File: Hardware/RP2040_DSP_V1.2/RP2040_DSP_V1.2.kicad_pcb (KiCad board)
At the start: 2 copper layers, 168.7 x 136.6 mm, 104 parts, among them J1 DC, J10 MIDI OUT, J11 MIDI IN, J12 OUTPUT, J13 Main, J2 EXP1, J3 EXP_2, J4 Daughter, J5 SW1, J6 SW2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

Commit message: [3D] Models updated
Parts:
- U12: footprint RP2040_DSP_Project_Library:128x64OLED -> DMME_Library:128x64OLED
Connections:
- RV8 pad : GNDD -> (no net)

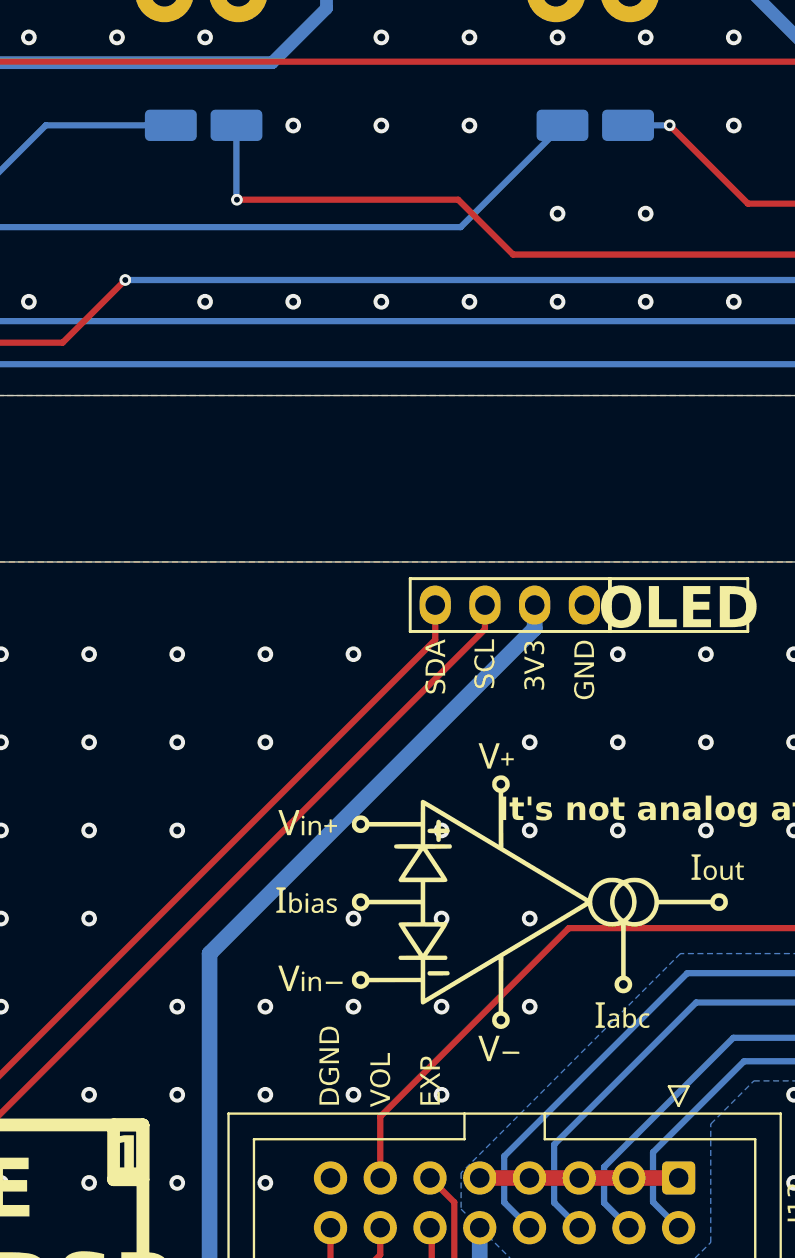
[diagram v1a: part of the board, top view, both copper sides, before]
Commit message: Added manufacturing files and BOM for V1.2
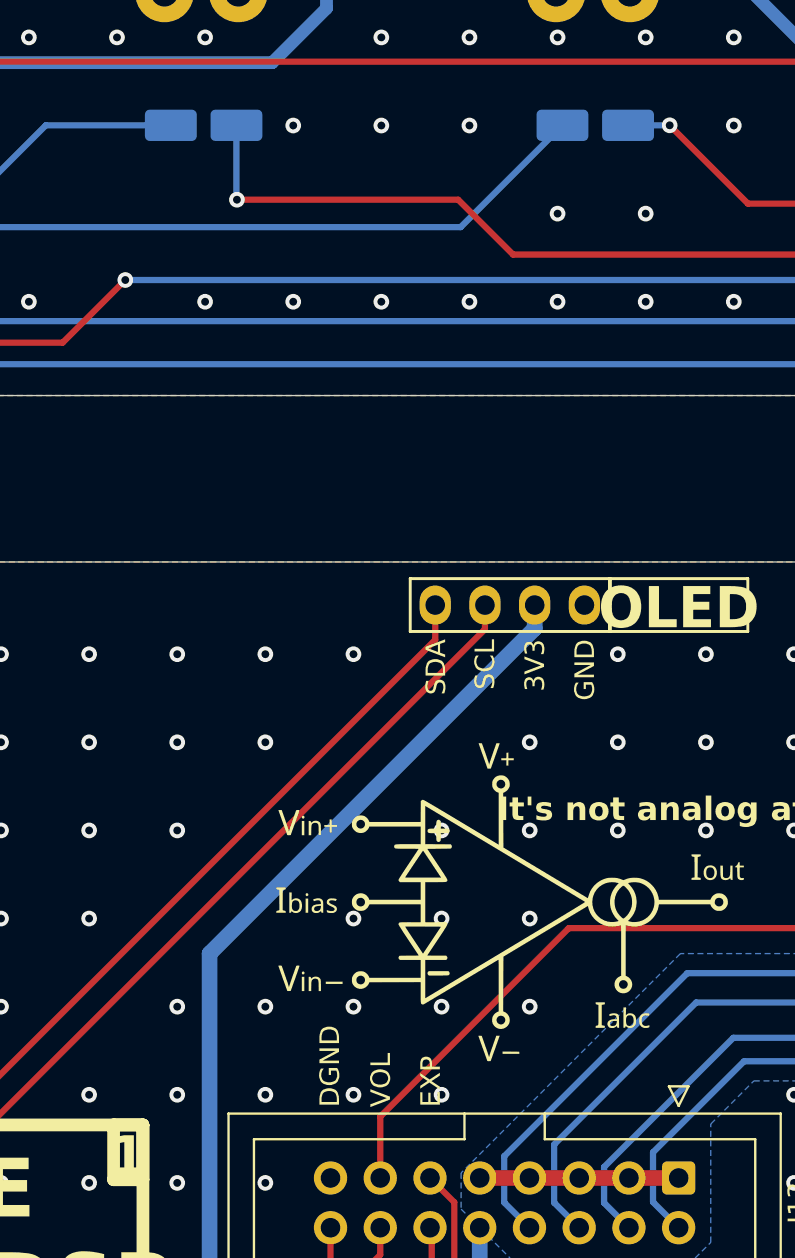
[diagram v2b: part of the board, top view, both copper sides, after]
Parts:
- U12: footprint DMME_Library:128x64OLED -> RP2040_DSP_Project_Library:128x64OLED
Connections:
- RV8 pad : (no net) -> GNDD

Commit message: V2.1 assembly files added
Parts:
- U12: footprint RP2040_DSP_Project_Library:128x64OLED -> DMME_Library:128x64OLED
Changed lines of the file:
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@@
 		)
 	)
-	(footprint "RP2040_DSP_Project_Library:128x64OLED"
+	(footprint "DMME_Library:128x64OLED"
 		(locked yes)
 		(layer "B.Cu")
@@
 			(pinfunction "GND")
 			(pintype "input")
-			(teardrops
-				(best_length_ratio 0.5)
-				(max_length 1)
-				(best_width_ratio 1)
-				(max_width 2)
-				(curved_edges yes)
-				(filter_ratio 0.9)
-				(enabled yes)
-				(allow_two_segments yes)
-				(prefer_zone_connections yes)
-			)
 		)
 		(pad "2" thru_hole oval
@@
 			(pinfunction "VCC")
 			(pintype "input")
-			(teardrops
-				(best_length_ratio 0.5)
-				(max_length 1)
-				(best_width_ratio 1)
-				(max_width 2)
-				(curved_edges yes)
-				(filter_ratio 0.9)
-				(enabled yes)
-				(allow_two_segments yes)
-				(prefer_zone_connections yes)
-			)
 		)
 		(pad "3" thru_hole oval
@@
 			(pinfunction "DCL")
 			(pintype "input")
-			(teardrops
-				(best_length_ratio 0.5)
-				(max_length 1)
-				(best_width_ratio 1)
-				(max_width 2)
-				(curved_edges yes)
-				(filter_ratio 0.9)
-				(enabled yes)
-				(allow_two_segments yes)
-				(prefer_zone_connections yes)
-			)
 		)
 		(pad "4" thru_hole oval
@@
 			(pinfunction "SDA")
 			(pintype "input")
-			(teardrops
-				(best_length_ratio 0.5)
-				(max_length 1)
-				(best_width_ratio 1)
-				(max_width 2)
-				(curved_edges yes)
-				(filter_ratio 0.9)
-				(enabled yes)
-				(allow_two_segments yes)
-				(prefer_zone_connections yes)
-			)
 		)
 		(embedded_fonts no)
-		(model "${DMME_3D_MODELS}/Pantalla OLED 0.96'' 128x64.stp"
+		(model "${DMME_3D_MODELS}/Display/Pantalla OLED 0.96'' 128x64.stp"
 			(offset
 				(xyz 0.2 -1.5 5.5)
@@
 	)
 	(zone
-		(net 22)
-		(net_name "/I2C_SDA")
-		(layer "F.Cu")
-		(name "$teardrop_padvia$")
-		(hatch none 0.1)
-		(priority 30093)
-		(attr
-			(teardrop
-				(type padvia)
-			)
-		)
-		(connect_pads yes
-			(clearance 0)
-		)
-		(min_thickness 0.0254)
-		(filled_areas_thickness no)
-		(fill yes
-			(thermal_gap 0.5)
-			(thermal_bridge_width 0.5)
-			(island_removal_mode 1)
-			(island_area_min 10)
-		)
-		(polygon
-			(pts
-				(xy 111.334066 71.595457) (xy 111.354985 71.384353) (xy 111.425681 71.087983) (xy 111.477812 70.93456)
-				(xy 111.540281 70.785297) (xy 111.602909 70.662804) (xy 111.672464 70.552196) (xy 111.735224 70.472211)
-				(xy 111.802184 70.405576) (xy 111.891676 70.344456) (xy 111.227207 69.699293) (xy 110.561324 70.344456)
-				(xy 110.683487 70.428088) (xy 110.80573 70.558517) (xy 110.923019 70.739309) (xy 111.023876 70.963322)
-				(xy 111.063016 71.084565) (xy 111.090323 71.200087) (xy 111.107793 71.369184)
-			)
-		)
-	)
-	(zone
 		(net 60)
 		(net_name "Net-(D6-A)")
@@
 	)
 	(zone
-		(net 21)
-		(net_name "/I2C_SCL")
-		(layer "F.Cu")
-		(name "$teardrop_padvia$")
-		(hatch none 0.1)
-		(priority 30073)
-		(attr
-			(teardrop
-				(type padvia)
-			)
-		)
-		(connect_pads yes
-			(clearance 0)
-		)
-		(min_thickness 0.0254)
-		(filled_areas_thickness no)
-		(fill yes
-			(thermal_gap 0.5)
-			(thermal_bridge_width 0.5)
-			(island_removal_mode 1)
-			(island_area_min 10)
-		)
-		(polygon
-			(pts
-				(xy 113.492229 71.437295) (xy 113.631072 71.219557) (xy 113.811116 70.963984) (xy 113.955245 70.77989)
-				(xy 114.106507 70.608599) (xy 114.217414 70.499936) (xy 114.326941 70.409995) (xy 114.431676 70.344456)
-				(xy 113.767207 69.699293) (xy 112.981872 70.056072) (xy 113.112724 70.185124) (xy 113.218455 70.342546)
-				(xy 113.295793 70.525374) (xy 113.339724 70.725598) (xy 113.345571 70.926702) (xy 113.333981 71.019371)
-				(xy 113.313291 71.103762) (xy 113.265955 71.211021)
-			)
-		)
-	)
-	(zone
 		(net 12)
 		(net_name "/R_ADC")
@@
 			)
 		)
-	)
-	(zone
-		(net 5)
-		(net_name "+3V3")
-		(layer "B.Cu")
-		(name "$teardrop_padvia$")
-		(hatch none 0.1)
-		(priority 30028)
-		(attr
-			(teardrop
-				(type padvia)
-			)
-		)
-		(connect_pads yes
-			(clearance 0)
-		)
-		(min_thickness 0.0254)
-		(filled_areas_thickness no)
-		(fill yes
-			(thermal_gap 0.5)
-			(thermal_bridge_width 0.5)
-			(island_removal_mode 1)
-			(island_area_min 10)
-		)
-		(polygon
-			(pts
-				(xy 116.173651 71.595285) (xy 116.287939 71.392636) (xy 116.385188 71.195655) (xy 116.513332 70.937583)
-				(xy 116.652411 70.68965) (xy 116.726196 70.579385) (xy 116.802889 70.483532) (xy 116.882548 70.406051)
-				(xy 116.96523 70.350901) (xy 116.307207 69.699293) (xy 115.5065 69.9) (xy 115.573153 69.97218) (xy 115.628643 70.046242)
-				(xy 115.710608 70.20229) (xy 115.755771 70.368183) (xy 115.765195 70.543622) (xy 115.738439 70.725806)
-				(xy 115.67616 70.90549) (xy 115.607965 71.029599)
-			)
-		)
